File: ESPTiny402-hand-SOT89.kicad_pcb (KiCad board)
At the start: 2 copper layers, 26.4 x 23.9 mm, 21 parts, among them J1 Conn_01x10_Male, J2 Conn_01x10_Male, J3 Conn_01x04_Male, U1 ESP-01v090, U2 ATtiny402-SS, U3 MCP1700

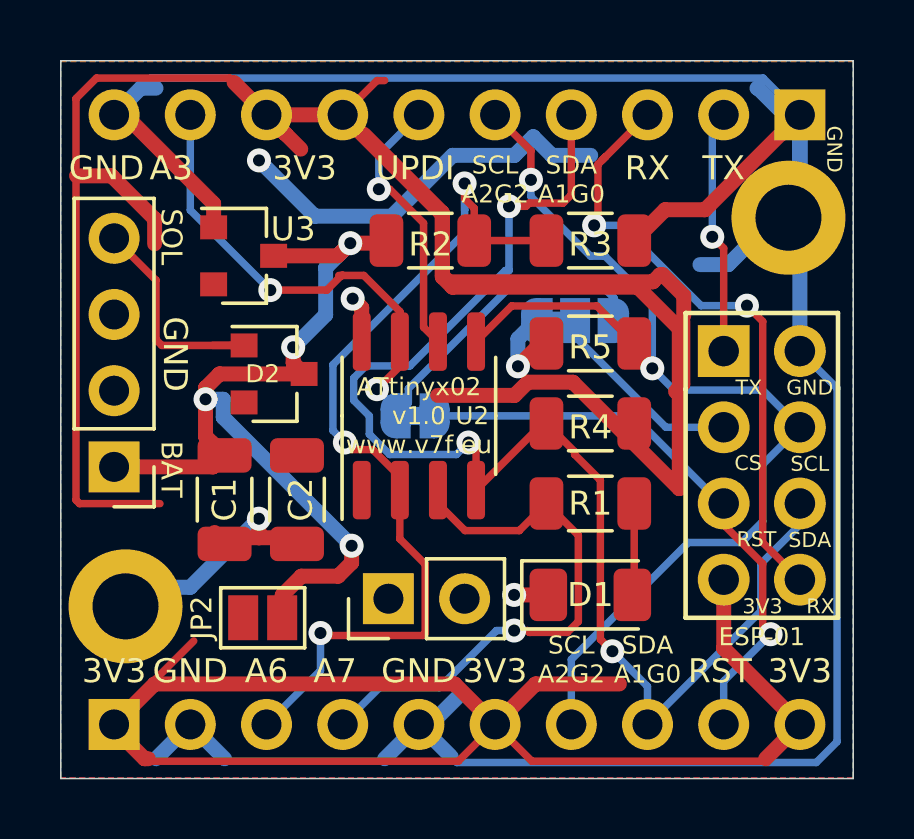
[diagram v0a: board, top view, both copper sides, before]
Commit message: Update for KiCad 9.0
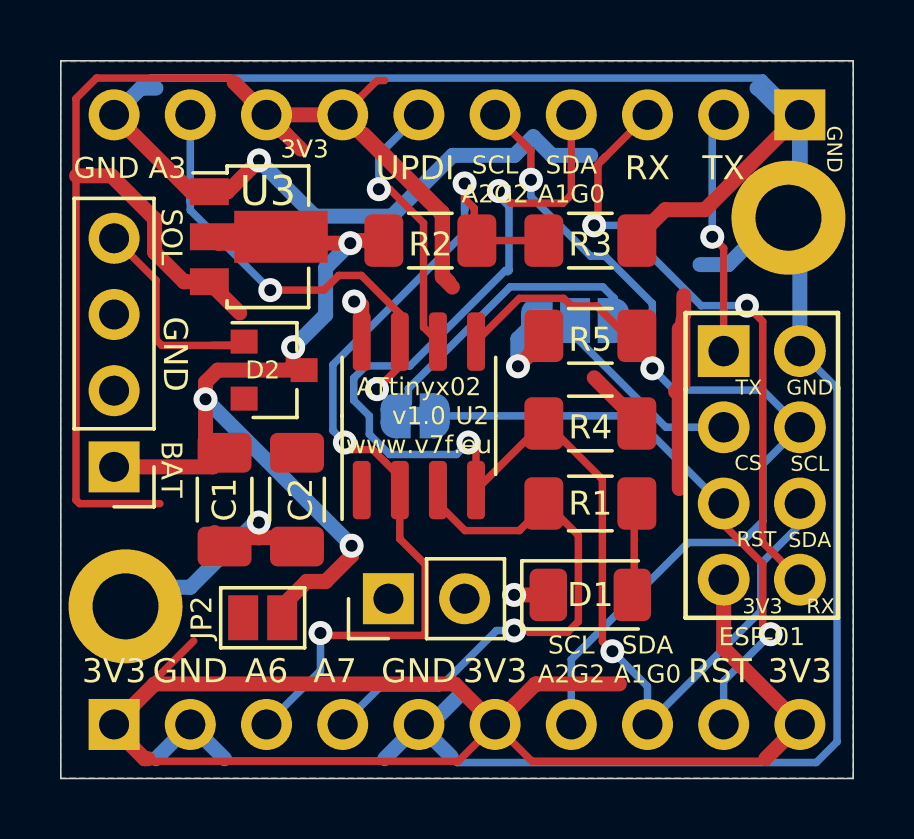
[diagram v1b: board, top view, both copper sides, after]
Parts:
- C1, C2: footprint Capacitor_SMD:C_1206_3216Metric -> Capacitor_SMD:C_1206_3216Metric_Pad1.33x1.80mm_HandSolder
- R1, R2, R3, R4, R5: footprint Resistor_SMD:R_1206_3216Metric -> Resistor_SMD:R_1206_3216Metric_Pad1.30x1.75mm_HandSolder
- U3: footprint Package_TO_SOT_SMD:SOT-23 -> Package_TO_SOT_SMD:SOT-89-3
- moved U3 0.81 mm to (52.3, 46.2)
- moved R5 0.25 mm to (63.4, 49.5)
- moved D2 0.13 mm to (52.8, 50.7)
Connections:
- U3 pad 2: +3V3 -> +BATT
- U3 pad 3: +BATT -> +3V3
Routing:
- net +3V3: track 139.0 -> 119.1 mm
- net +BATT: track 31.7 -> 33.1 mm
- net GND: track 123.1 -> 124.4 mm
- net /SDA-A1: track 46.2 -> 46.8 mm

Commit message: Minor cosmetic cleanups
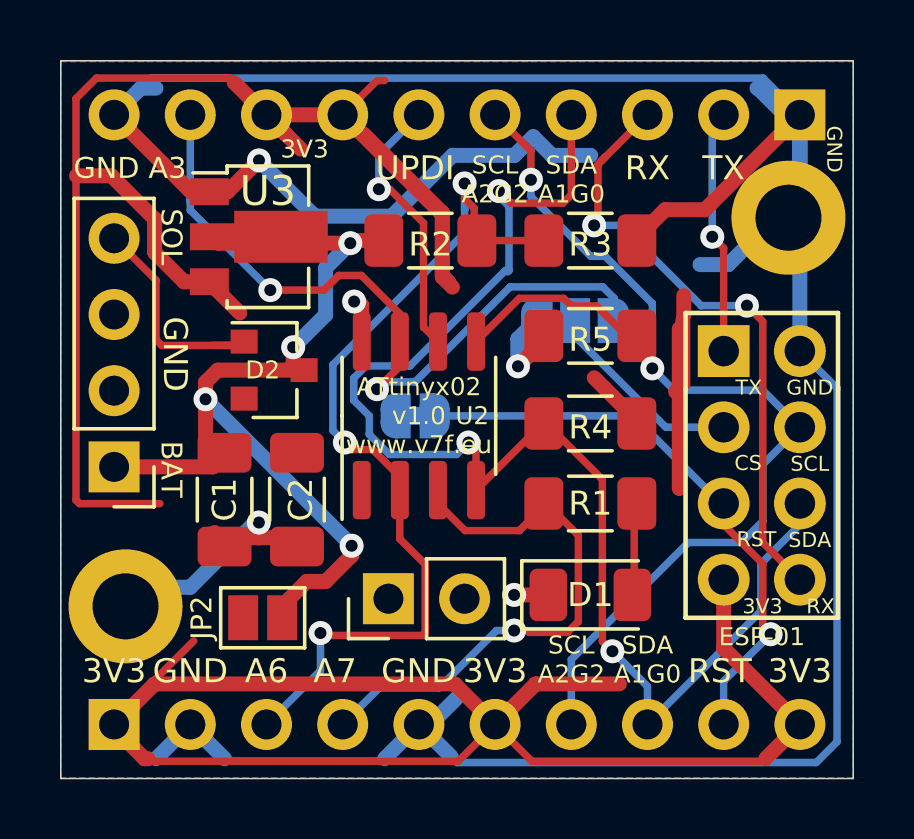
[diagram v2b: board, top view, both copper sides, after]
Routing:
- net /A3: track 27.6 -> 28.1 mm
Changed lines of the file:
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@@
 		(0 "F.Cu" signal)
 		(2 "B.Cu" signal)
-		(9 "F.Adhes" user)
-		(11 "B.Adhes" user)
+		(9 "F.Adhes" user "F.Adhesive")
+		(11 "B.Adhes" user "B.Adhesive")
 		(13 "F.Paste" user)
 		(15 "B.Paste" user)
-		(5 "F.SilkS" user)
-		(7 "B.SilkS" user)
+		(5 "F.SilkS" user "F.Silkscreen")
+		(7 "B.SilkS" user "B.Silkscreen")
 		(1 "F.Mask" user)
 		(3 "B.Mask" user)
-		(17 "Dwgs.User" user)
-		(19 "Cmts.User" user)
-		(21 "Eco1.User" user)
-		(23 "Eco2.User" user)
+		(17 "Dwgs.User" user "User.Drawings")
+		(19 "Cmts.User" user "User.Comments")
+		(21 "Eco1.User" user "User.Eco1")
+		(23 "Eco2.User" user "User.Eco2")
 		(25 "Edge.Cuts" user)
 		(27 "Margin" user)
-		(31 "F.CrtYd" user)
-		(29 "B.CrtYd" user)
+		(31 "F.CrtYd" user "F.Courtyard")
+		(29 "B.CrtYd" user "B.Courtyard")
 		(35 "F.Fab" user)
 		(33 "B.Fab" user)
@@
 	)
 	(segment
-		(start 50.038 42.487998)
-		(end 50.038 42.164)
+		(start 57.531654 51.066)
+		(end 56.503 51.066)
 		(width 0.25)
 		(layer "B.Cu")
@@
 	)
 	(segment
-		(start 57.30599 51.77201)
-		(end 56.881 52.197)
+		(start 50.038 42.487998)
+		(end 50.038 42.164)
 		(width 0.25)
 		(layer "B.Cu")
@@
 	)
 	(segment
-		(start 60.700664 47.89699)
-		(end 57.30599 51.291664)
+		(start 56.881 52.197)
+		(end 56.881 51.928)
 		(width 0.25)
 		(layer "B.Cu")
@@
 	)
 	(segment
-		(start 56.881 52.197)
-		(end 56.881 51.928)
+		(start 50.038 45.339)
+		(end 50.038 44.958)
 		(width 0.25)
 		(layer "B.Cu")
@@
 	)
 	(segment
-		(start 50.038 45.339)
-		(end 50.038 44.958)
+		(start 60.700664 47.89699)
+		(end 57.531654 51.066)
 		(width 0.25)
 		(layer "B.Cu")
@@
 	)
 	(segment
-		(start 50.038 42.164)
-		(end 50.038 44.958)
+		(start 56.881 51.652999)
+		(end 56.881 52.197)
 		(width 0.25)
 		(layer "B.Cu")
@@
 	)
 	(segment
-		(start 64.165 49.022)
-		(end 64.165 48.274408)
+		(start 56.503 51.066)
+		(end 56.261 51.308)
+		(width 0.25)
+		(layer "B.Cu")
+		(net 10)
+	)
+	(segment
+		(start 50.038 42.164)
+		(end 50.038 44.958)
 		(width 0.25)
 		(layer "B.Cu")
@@
 	)
 	(segment
-		(start 57.30599 51.291664)
-		(end 57.30599 51.77201)
+		(start 64.165 49.022)
+		(end 64.165 48.274408)
 		(width 0.25)
 		(layer "B.Cu")
@@
 	)
 	(segment
-		(start 58.909001 53.485999)
-		(end 56.685951 53.485999)
-		(width 0.25)
-		(layer "B.Cu")
-		(net 13)
-	)
-	(segment
 		(start 69.056601 58.705399)
 		(end 65.278 62.484)
@@
 	)
 	(segment
-		(start 56.685951 53.485999)
-		(end 56.00599 52.806038)
+		(start 59.309 53.086)
+		(end 58.909001 53.485999)
 		(width 0.25)
 		(layer "B.Cu")
@@
 	)
 	(segment
-		(start 59.309 53.086)
-		(end 58.909001 53.485999)
+		(start 56.674077 53.485999)
+		(end 56.000053 52.811975)
+		(width 0.25)
+		(layer "B.Cu")
+		(net 13)
+	)
+	(segment
+		(start 58.909001 53.485999)
+		(end 56.674077 53.485999)
 		(width 0.25)
 		(layer "B.Cu")
